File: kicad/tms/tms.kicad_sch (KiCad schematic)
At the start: 18 parts, among them J1 Conn_01x03, Q2 BT169B, SW1 SW_DIP_x01, SW2 SW_DIP_x01, SW3 SW_DIP_x01

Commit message: Kicad files
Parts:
- added C6: 0.33μF, symbol Device:C
- added C7: 0.1μF, symbol Device:C
- added U4: L7812CV, symbol Regulator_Linear:L7812
- C3: value C -> 0.22μF
- J1: value Conn_01x03 -> 120V @ 60Hz
- R7: renamed from R10; value R -> 3x 10Ω
- renumbered C7 to C4, C8 to C5, D18 to D1, Q2 to Q1, R2 to R1,R2,R3, R14 to R10, R15 to R4,R5,R6, R9 to R8, R13 to R9
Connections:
- net GND: now also C6.2, C7.2, U4.2 (GND)
- net PSU 24V: now also C6.1, U4.1 (IN)
- new net PSU 12V: C7.1, U4.3 (OUT)
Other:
- note added: "L1"
- moved on the sheet: C4, C5, J1, SW1, SW2, SW3

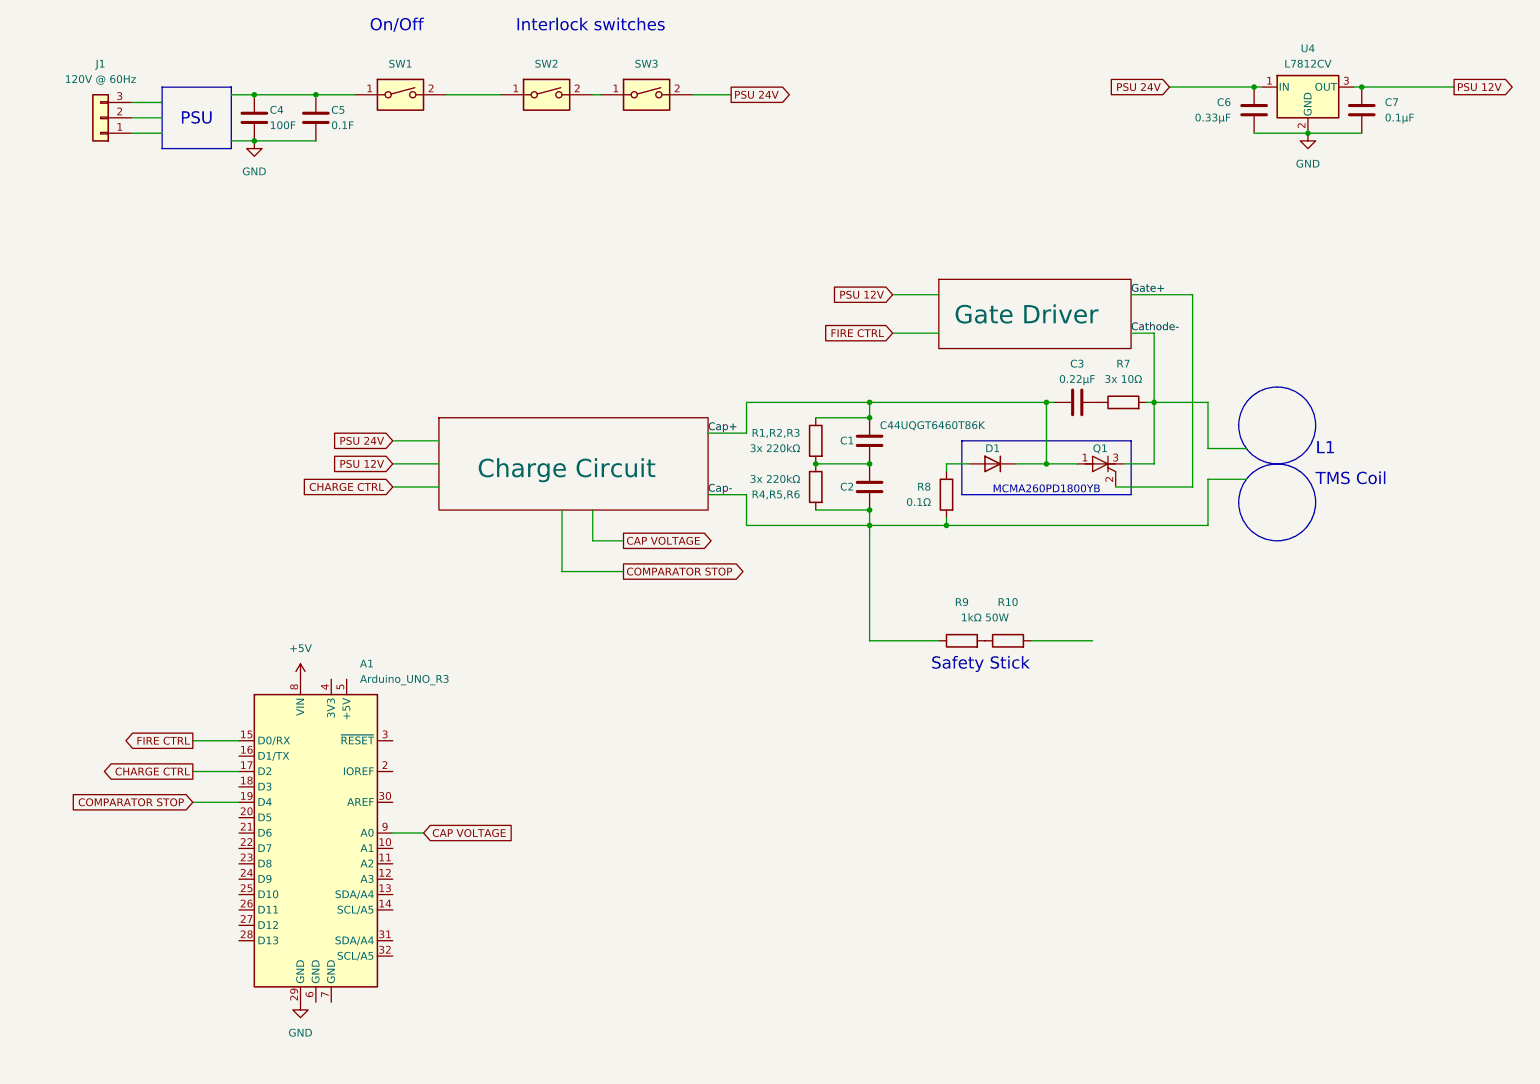
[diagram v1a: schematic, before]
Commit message: Schematic fixes after real life tests
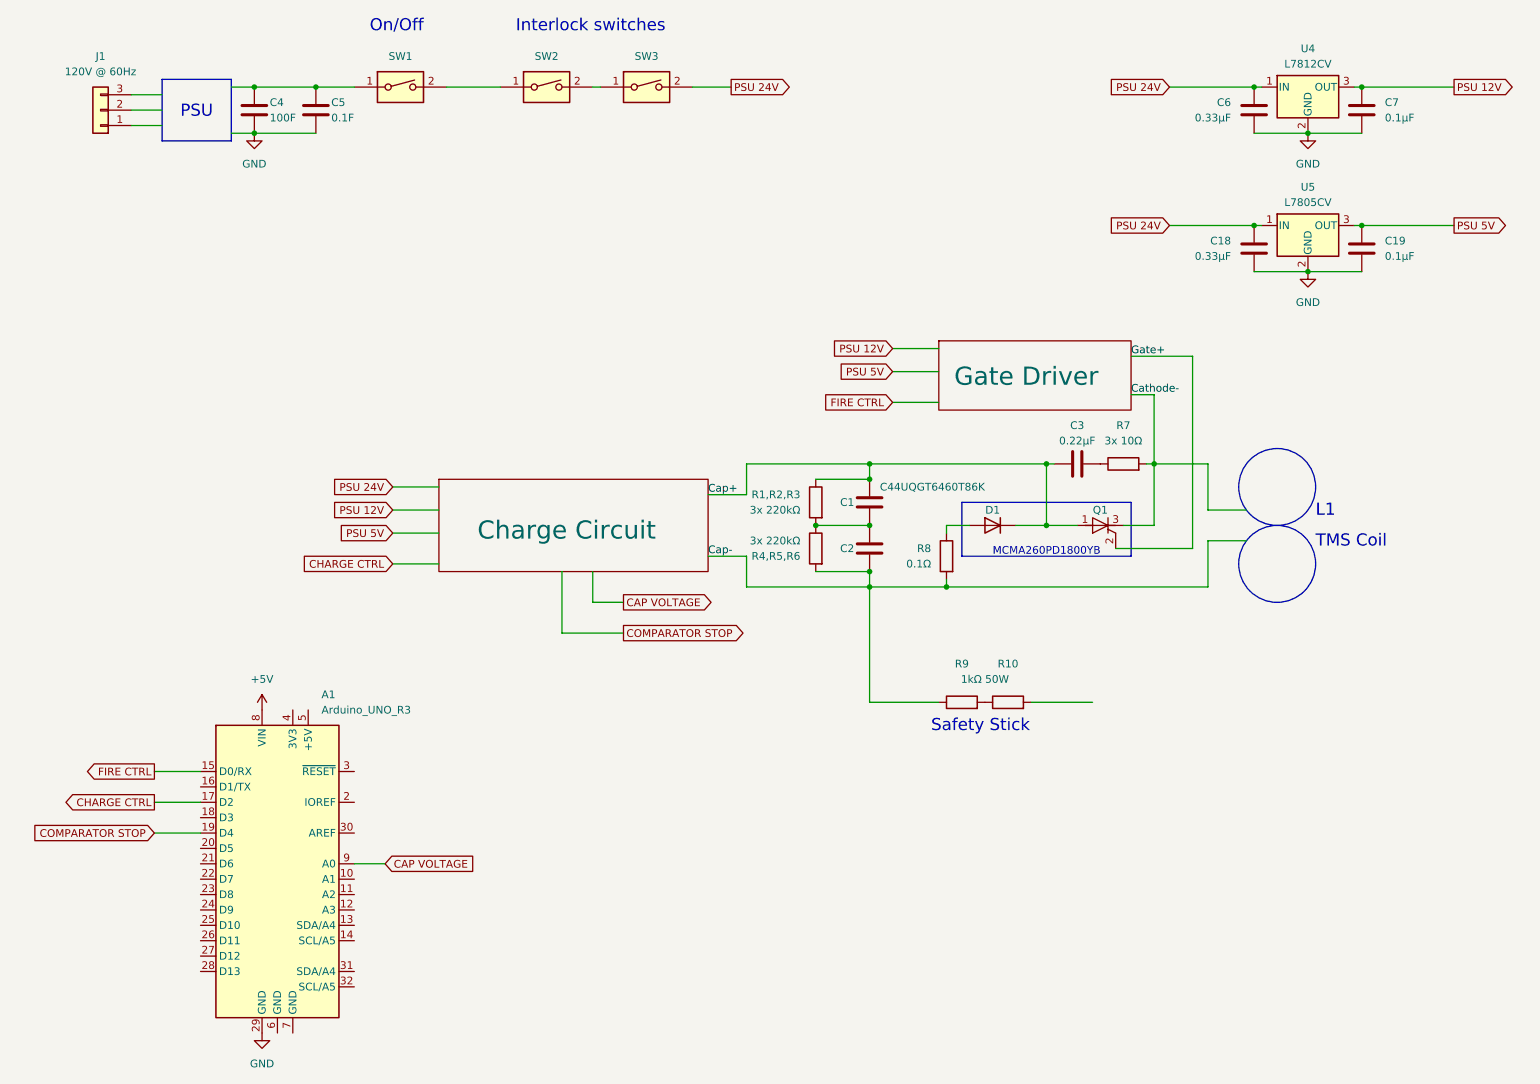
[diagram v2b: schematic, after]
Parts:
- added C18: 0.33μF, symbol Device:C
- added C19: 0.1μF, symbol Device:C
- added U5: L7805CV, symbol Regulator_Linear:L7812
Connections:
- net GND: now also C18.2, C19.2, U5.2 (GND)
- net PSU 24V: now also C18.1, U5.1 (IN)
- new net PSU 5V: C19.1, U5.3 (OUT)
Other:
- moved on the sheet: A1, C1, C2, C3, C4, C5, D1, J1, Q1, R1,R2,R3, R10, R4,R5,R6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

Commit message: Fixed TMS schematic
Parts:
- C4: value 100F -> 100 uF
- C5: value 0.1F -> 0.1 uF
- renumbered C18 to C8, C19 to C9, R8 to R10, R9 to R11, R10 to R12, R7 to R7,R8,R9, U4 to U1, U5 to U2
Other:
- moved on the sheet: C5
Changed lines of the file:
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@@
   (junction (at 186.69 93.98) (diameter 0) (color 0 0 0 0)
   )
-  (junction (at 66.04 31.75) (diameter 0) (color 0 0 0 0)
-  )
   (junction (at 157.48 114.3) (diameter 0) (color 0 0 0 0)
   )
@@
   (junction (at 238.76 54.61) (diameter 0) (color 0 0 0 0)
   )
+  (junction (at 68.58 31.75) (diameter 0) (color 0 0 0 0)
+  )
   (junction (at 157.48 93.98) (diameter 0) (color 0 0 0 0)
   )
@@
     (stroke (width 0) (type default))
   )
-  (wire (pts (xy 66.04 31.75) (xy 72.39 31.75))
+  (wire (pts (xy 55.88 31.75) (xy 68.58 31.75))
     (stroke (width 0) (type default))
   )
@@
     (stroke (width 0) (type default))
   )
-  (wire (pts (xy 55.88 31.75) (xy 66.04 31.75))
-    (stroke (width 0) (type default))
-  )
   (wire (pts (xy 207.01 54.61) (xy 220.98 54.61))
     (stroke (width 0) (type default))
@@
     (stroke (width 0) (type default))
   )
-  (wire (pts (xy 55.88 39.37) (xy 66.04 39.37))
+  (wire (pts (xy 55.88 39.37) (xy 68.58 39.37))
     (stroke (width 0) (type default))
   )
@@
   )
   (wire (pts (xy 130.81 99.06) (xy 137.16 99.06))
+    (stroke (width 0) (type default))
+  )
+  (wire (pts (xy 68.58 31.75) (xy 72.39 31.75))
     (stroke (width 0) (type default))
   )
@@
   (symbol (lib_id "Regulator_Linear:L7812") (at 229.87 31.75 0) (unit 1)
     (in_bom yes) (on_board yes) (dnp no) (fields_autoplaced)
-    (property "Reference" "U4" (at 229.87 25.4 0)
+    (property "Reference" "U1" (at 229.87 25.4 0)
       (effects (font (size 1.27 1.27)))
     )
@@
       (project "tms"
         (path "/dc88686f-c772-4c63-b1cc-83a281c6b46c"
-          (reference "U4") (unit 1)
+          (reference "U1") (unit 1)
         )
       )
@@
   (symbol (lib_id "Device:R") (at 170.18 109.22 0) (mirror y) (unit 1)
     (in_bom yes) (on_board yes) (dnp no)
-    (property "Reference" "R8" (at 167.64 107.95 0)
+    (property "Reference" "R10" (at 167.64 107.95 0)
       (effects (font (size 1.27 1.27)) (justify left))
     )
@@
       (project "tms"
         (path "/dc88686f-c772-4c63-b1cc-83a281c6b46c"
-          (reference "R8") (unit 1)
+          (reference "R10") (unit 1)
         )
       )
@@
   (symbol (lib_id "Device:R") (at 199.39 93.98 90) (unit 1)
     (in_bom yes) (on_board yes) (dnp no)
-    (property "Reference" "R7" (at 199.39 87.63 90)
+    (property "Reference" "R7,R8,R9" (at 199.39 87.63 90)
       (effects (font (size 1.27 1.27)))
     )
@@
       (project "tms"
         (path "/dc88686f-c772-4c63-b1cc-83a281c6b46c"
-          (reference "R7") (unit 1)
+          (reference "R7,R8,R9") (unit 1)
         )
       )
@@
       (effects (font (size 1.27 1.27)) (justify left))
     )
-    (property "Value" "100F" (at 58.42 36.83 0)
+    (property "Value" "100 uF" (at 58.42 36.83 0)
       (effects (font (size 1.27 1.27)) (justify left))
     )
@@
   (symbol (lib_id "Device:C") (at 238.76 58.42 0) (unit 1)
     (in_bom yes) (on_board yes) (dnp no)
-    (property "Reference" "C19" (at 242.57 57.15 0)
+    (property "Reference" "C9" (at 242.57 57.15 0)
       (effects (font (size 1.27 1.27)) (justify left))
     )
@@
       (project "tms"
         (path "/dc88686f-c772-4c63-b1cc-83a281c6b46c"
-          (reference "C19") (unit 1)
+          (reference "C9") (unit 1)
         )
       )
@@
   (symbol (lib_id "Regulator_Linear:L7812") (at 229.87 54.61 0) (unit 1)
     (in_bom yes) (on_board yes) (dnp no) (fields_autoplaced)
-    (property "Reference" "U5" (at 229.87 48.26 0)
+    (property "Reference" "U2" (at 229.87 48.26 0)
       (effects (font (size 1.27 1.27)))
     )
@@
       (project "tms"
         (path "/dc88686f-c772-4c63-b1cc-83a281c6b46c"
-          (reference "U5") (unit 1)
+          (reference "U2") (unit 1)
         )
       )
@@
   (symbol (lib_id "Device:R") (at 180.34 133.35 90) (unit 1)
     (in_bom yes) (on_board yes) (dnp no)
-    (property "Reference" "R10" (at 180.34 127 90)
+    (property "Reference" "R12" (at 180.34 127 90)
       (effects (font (size 1.27 1.27)))
     )
@@
       (project "tms"
         (path "/dc88686f-c772-4c63-b1cc-83a281c6b46c"
-          (reference "R10") (unit 1)
+          (reference "R12") (unit 1)
         )
       )
@@
   (symbol (lib_id "Device:C") (at 220.98 58.42 0) (mirror y) (unit 1)
     (in_bom yes) (on_board yes) (dnp no)
-    (property "Reference" "C18" (at 217.17 57.15 0)
+    (property "Reference" "C8" (at 217.17 57.15 0)
       (effects (font (size 1.27 1.27)) (justify left))
     )
@@
       (project "tms"
         (path "/dc88686f-c772-4c63-b1cc-83a281c6b46c"
-          (reference "C18") (unit 1)
+          (reference "C8") (unit 1)
         )
       )
@@
   (symbol (lib_id "Device:R") (at 172.72 133.35 90) (unit 1)
     (in_bom yes) (on_board yes) (dnp no)
-    (property "Reference" "R9" (at 172.72 127 90)
+    (property "Reference" "R11" (at 172.72 127 90)
       (effects (font (size 1.27 1.27)))
     )
@@
       (project "tms"
         (path "/dc88686f-c772-4c63-b1cc-83a281c6b46c"
-          (reference "R9") (unit 1)
+          (reference "R11") (unit 1)
         )
       )
@@
     )
   )
-  (symbol (lib_id "Device:C") (at 66.04 35.56 0) (unit 1)
-    (in_bom yes) (on_board yes) (dnp no)
-    (property "Reference" "C5" (at 68.58 34.29 0)
-      (effects (font (size 1.27 1.27)) (justify left))
-    )
-    (property "Value" "0.1F" (at 68.58 36.83 0)
-      (effects (font (size 1.27 1.27)) (justify left))
-    )
-    (property "Footprint" "" (at 67.0052 39.37 0)
-      (effects (font (size 1.27 1.27)) hide)
-    )
-    (property "Datasheet" "~" (at 66.04 35.56 0)
-      (effects (font (size 1.27 1.27)) hide)
-    )
+  (symbol (lib_id "Device:C") (at 68.58 35.56 0) (unit 1)
+    (in_bom yes) (on_board yes) (dnp no)
+    (property "Reference" "C5" (at 71.12 34.29 0)
+      (effects (font (size 1.27 1.27)) (justify left))
+    )
+    (property "Value" "0.1 uF" (at 71.12 36.83 0)
+      (effects (font (size 1.27 1.27)) (justify left))
+    )
+    (property "Footprint" "" (at 69.5452 39.37 0)
+      (effects (font (size 1.27 1.27)) hide)
+    )
+    (property "Datasheet" "~" (at 68.58 35.56 0)
+      (effects (font (size 1.27 1.27)) hide)
+    )

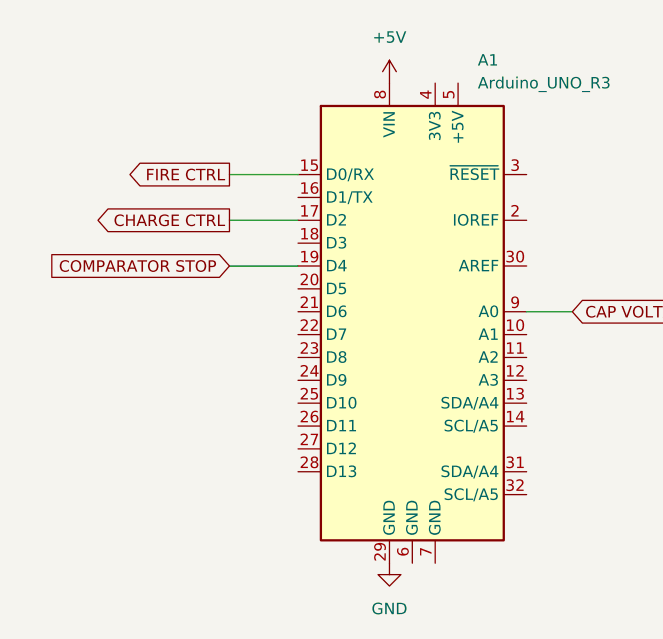
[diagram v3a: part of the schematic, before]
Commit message: Schematic changes
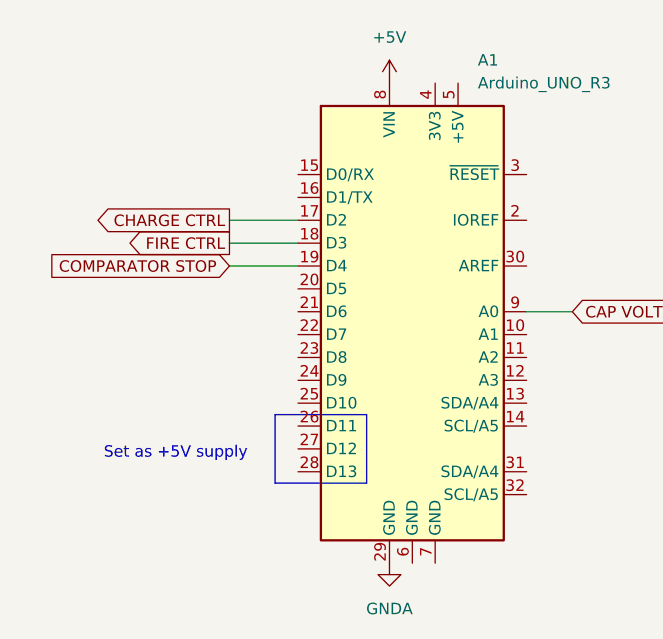
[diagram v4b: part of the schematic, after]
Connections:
- net FIRE CTRL: now also A1.18 (D3); no longer A1.15 (D0/RX)
- net GND: no longer A1.29 (GND)
- new net GNDA: A1.29 (GND)
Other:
- note added: "Set as +5V supply"
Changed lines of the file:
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@@
+    (stroke (width 0) (type default))
+  )
+  (wire (pts (xy 39.37 152.4) (xy 46.99 152.4))
     (stroke (width 0) (type default))
   )
@@
     (stroke (width 0) (type default))
   )
-  (wire (pts (xy 39.37 144.78) (xy 46.99 144.78))
-    (stroke (width 0) (type default))
-  )
   (wire (pts (xy 200.66 82.55) (xy 204.47 82.55))
     (stroke (width 0) (type default))
@@
   )
   (rectangle (start 172.72 100.33) (end 200.66 109.22)
+    (stroke (width 0) (type default))
+    (fill (type none))
+  )
+  (rectangle (start 44.45 171.45) (end 54.61 179.07)
     (stroke (width 0) (type default))
     (fill (type none))
@@
     (effects (font (size 2 2)) (justify left bottom))
   )
+  (text "Set as +5V supply" (at 25.4 176.53 0)
+    (effects (font (size 1.27 1.27)) (justify left bottom))
+  )
   (label "Cap-" (at 130.81 109.22 0) (fields_autoplaced)
     (effects (font (size 1.27 1.27)) (justify left bottom))
@@
     )
   )
-  (global_label "FIRE CTRL" (shape output) (at 39.37 144.78 180) (fields_autoplaced)
-    (effects (font (size 1.27 1.27)) (justify right))
-    (property "Intersheetrefs" "${INTERSHEET_REFS}" (at 26.7691 144.78 0)
+  (global_label "FIRE CTRL" (shape output) (at 39.37 152.4 180) (fields_autoplaced)
+    (effects (font (size 1.27 1.27)) (justify right))
+    (property "Intersheetrefs" "${INTERSHEET_REFS}" (at 26.7691 152.4 0)
       (effects (font (size 1.27 1.27)) (justify right) hide)
     )
@@
     )
   )
-  (symbol (lib_id "power:GND") (at 57.15 187.96 0) (unit 1)
-    (in_bom yes) (on_board yes) (dnp no) (fields_autoplaced)
-    (property "Reference" "#PWR01" (at 57.15 194.31 0)
-      (effects (font (size 1.27 1.27)) hide)
-    )
-    (property "Value" "GND" (at 57.15 193.04 0)
-      (effects (font (size 1.27 1.27)))
-    )
-    (property "Footprint" "" (at 57.15 187.96 0)
-      (effects (font (size 1.27 1.27)) hide)
-    )
-    (property "Datasheet" "" (at 57.15 187.96 0)
-      (effects (font (size 1.27 1.27)) hide)
-    )
-    (pin "1")
-    (instances
-      (project "tms"
-        (path "/dc88686f-c772-4c63-b1cc-83a281c6b46c"
-          (reference "#PWR01") (unit 1)
-        )
-      )
-    )
-  )
   (symbol (lib_id "Device:C") (at 157.48 100.33 0) (unit 1)
     (in_bom yes) (on_board yes) (dnp no)
@@
         )
       )
+    )
+  )
+  (symbol (lib_id "power:GNDA") (at 57.15 187.96 0) (unit 1)
+    (in_bom yes) (on_board yes) (dnp no) (fields_autoplaced)
+    (property "Reference" "#PWR01" (at 57.15 194.31 0)
+      (effects (font (size 1.27 1.27)) hide)
+    )
+    (property "Value" "GNDA" (at 57.15 193.04 0)
+      (effects (font (size 1.27 1.27)))
+    )
+    (property "Footprint" "" (at 57.15 187.96 0)
+      (effects (font (size 1.27 1.27)) hide)
+    )
+    (property "Datasheet" "" (at 57.15 187.96 0)
+      (effects (font (size 1.27 1.27)) hide)
+    )
+    (pin "1")
+    (instances
+      (project "tms"
+        (path "/dc88686f-c772-4c63-b1cc-83a281c6b46c"
+          (reference "#PWR01") (unit 1)
+        )
+      )
